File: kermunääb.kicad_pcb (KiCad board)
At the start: 2 copper layers, 140 parts, among them J1 Conn_01x05, SW1 RotaryEncoder_Switch, SW10 SW_SPST, SW11 SW_SPST, SW12 SW_SPST, SW13 SW_SPST, SW14 SW_SPST, SW15 SW_SPST, SW16 SW_SPST, SW17 SW_SPST, SW18 SW_SPST, SW19 SW_SPST, SW2 SW_SPST, SW20 SW_SPST, SW21 SW_SPST, SW22 SW_SPST, SW23 SW_SPST, SW24 SW_SPST, SW25 SW_SPST, SW26 SW_SPST, SW27 SW_SPST, SW28 SW_SPST, SW29 SW_SPST, SW3 SW_SPST, SW30 SW_SPST, SW31 SW_SPST, SW32 SW_SPST, SW33 SW_SPST, SW33A1 SW_SPST, SW34 SW_SPST, SW35 SW_SPST, SW36 SW_SPST, SW37 SW_SPST, SW38 SW_SPST, SW39 SW_SPST, SW4 SW_SPST, SW40 SW_SPST, SW41 SW_SPST, SW42 SW_SPST, SW43 SW_SPST, SW44 SW_SPST, SW45 SW_SPST, SW46 SW_SPST, SW47 SW_SPST, SW48 SW_SPST, SW49 SW_SPST, SW5 SW_SPST, SW50 SW_SPST, SW51 SW_SPST, SW52 SW_SPST, SW53 SW_SPST, SW54 SW_SPST, SW55 SW_SPST, SW56 SW_SPST, SW57 SW_SPST, SW58 SW_SPST, SW59 SW_SPST, SW6 SW_SPST, SW60 SW_SPST, SW61 SW_SPST, SW62 SW_SPST, SW63 SW_SPST, SW64 SW_SPST, SW65 SW_SPST, SW7 SW_SPST, SW8 SW_SPST, SW9 SW_SPST, U1 ProMicro

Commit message: change footprint for rotary header & add silk
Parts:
- J1: footprint Connector_PinSocket_2.54mm:PinSocket_1x05_P2.54mm_Horizontal -> Connector_PinSocket_2.54mm:PinSocket_1x05_P2.54mm_Vertical
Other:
- board text added: "A"
- board text added: "B"
- board text added: "GND"
- board text added: "SW1"
- board text added: "SW2"

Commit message: initial routing for right half and tweaks
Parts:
- added U2: ProMicro, promicro:ProMicro, B.Cu at (246.4, 69.8)
- J1: footprint Connector_PinSocket_2.54mm:PinSocket_1x05_P2.54mm_Vertical -> Connector_PinSocket_2.54mm:PinSocket_1x05_P2.54mm_Horizontal
- moved D7 7.00 mm to (153.4, 64.8), turned to 0 degrees
- moved D9 4.95 mm to (265.4, 64.8), turned to 180 degrees
- moved D8 4.95 mm to (246.4, 64.8), turned to 180 degrees
- moved D20 3.46 mm to (144.8, 82.8)
- moved D21 1.25 mm to (158.8, 82.5)
- moved U1 0.63 mm to (148.9, 69.8)
- moved D10 0.55 mm to (281.0, 61.8)
- moved D11 0.55 mm to (300.0, 61.8)
- moved D12 0.55 mm to (319.1, 61.8)
- moved D13 0.55 mm to (338.1, 61.8)
- moved D14 0.55 mm to (357.2, 61.8)
- renumbered SW33A1 to SW30A1
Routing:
- net /Col13: track 103.7 -> 202.7 mm
- net /Row5B: track 190.5 -> 279.3 mm
- net /Col12: track 149.3 -> 222.3 mm
- net /Row4B: track 121.4 -> 182.5 mm
- net /Col11: track 127.9 -> 182.4 mm
- net /Col10: track 123.9 -> 173.6 mm
- net /Row3B: track 114.3 -> 150.8 mm
- net /Col9: track 118.4 -> 145.3 mm
- net /Row1: track 109.4 -> 98.3 mm
- net Net-(D8-A): track 10.8 -> 2.70 mm
- net Net-(D9-A): track 10.8 -> 2.70 mm
- net Net-(D20-A): track 10.8 -> 2.96 mm
- net /Col5: track 105.3 -> 98.2 mm
- net /Col3: track 138.7 -> 143.9 mm
- net /Col4: track 141.2 -> 144.8 mm
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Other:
- board outline added: 148.2 x 105.2 mm

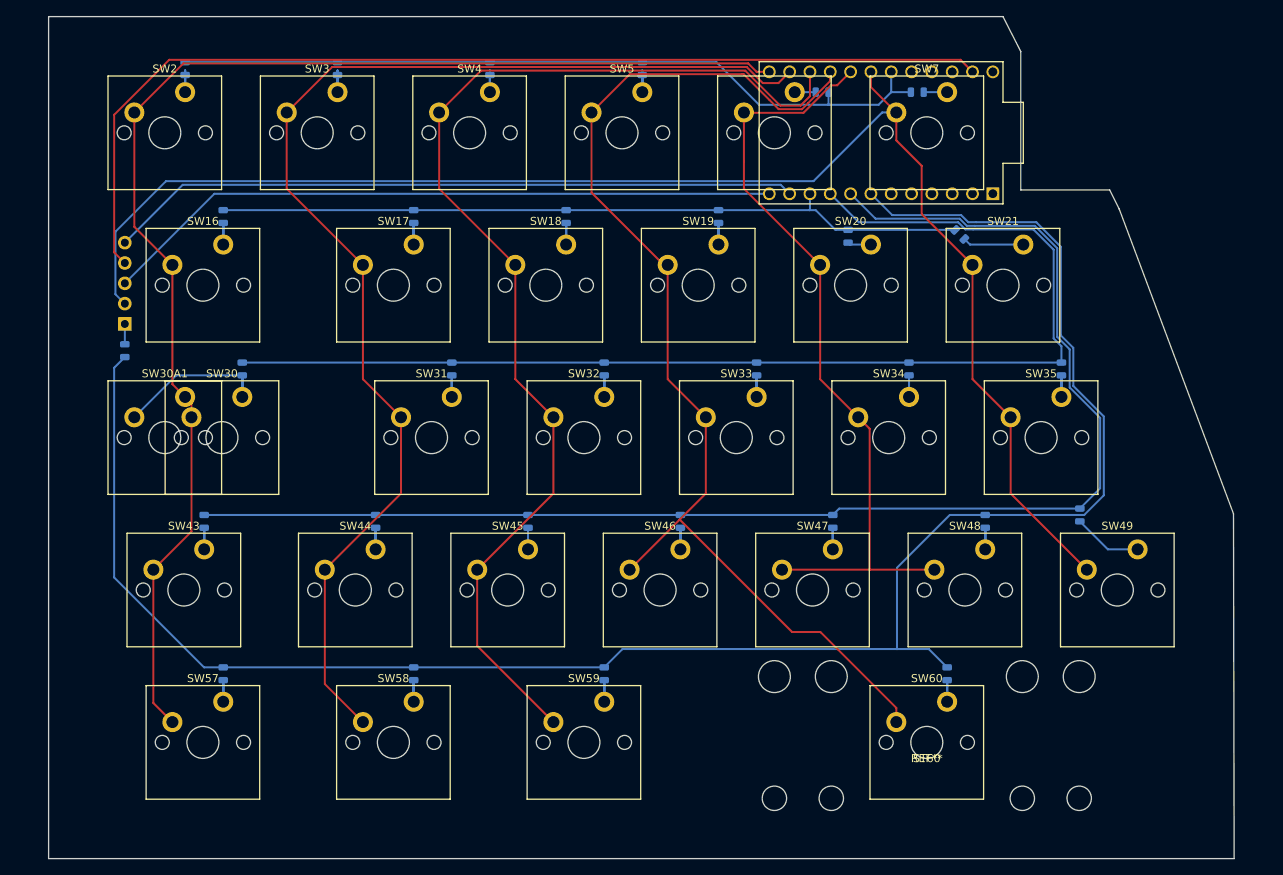
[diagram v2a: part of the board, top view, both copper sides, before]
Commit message: add initial edgecuts for left
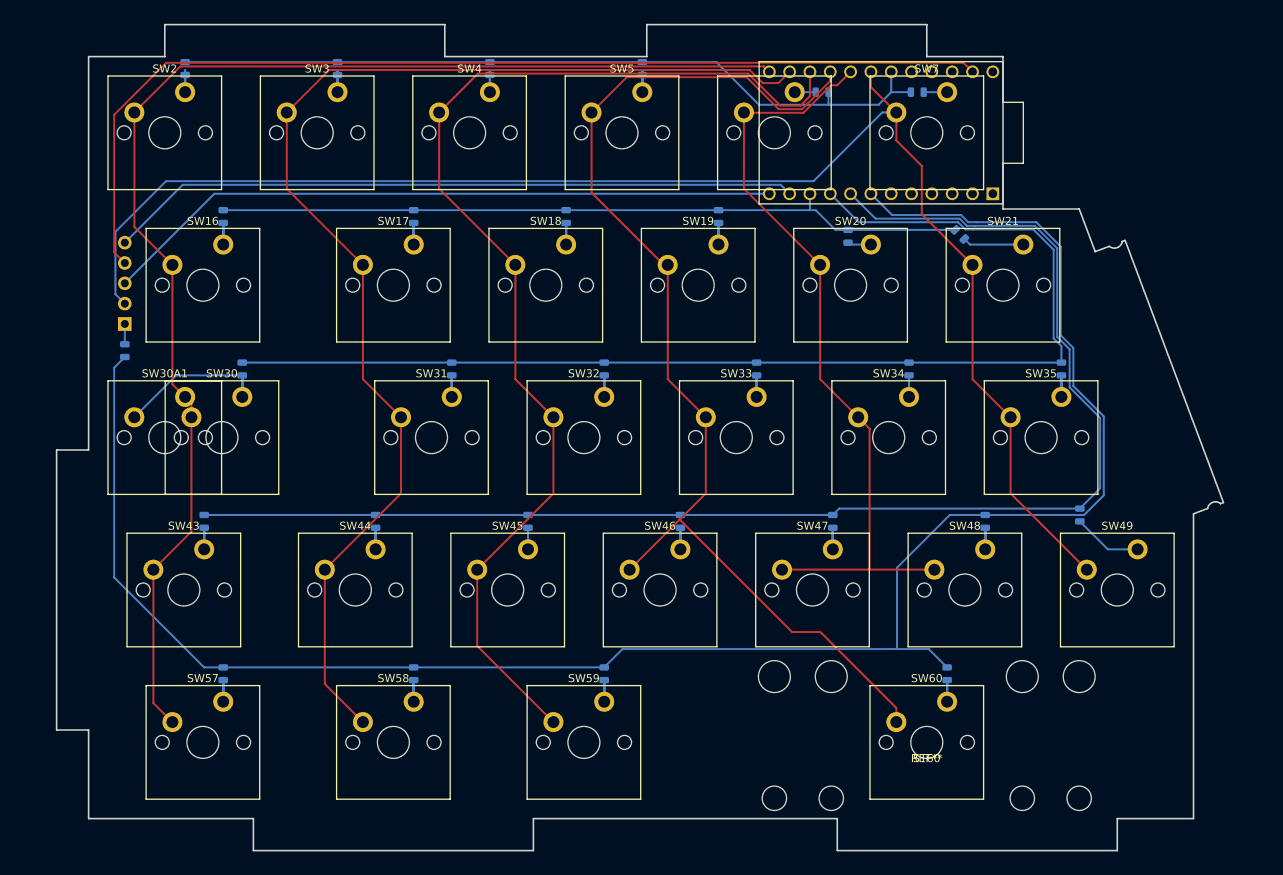
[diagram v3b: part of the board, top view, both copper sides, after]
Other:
- board size 148.2 x 105.2 mm -> 145.9 x 103.3 mm

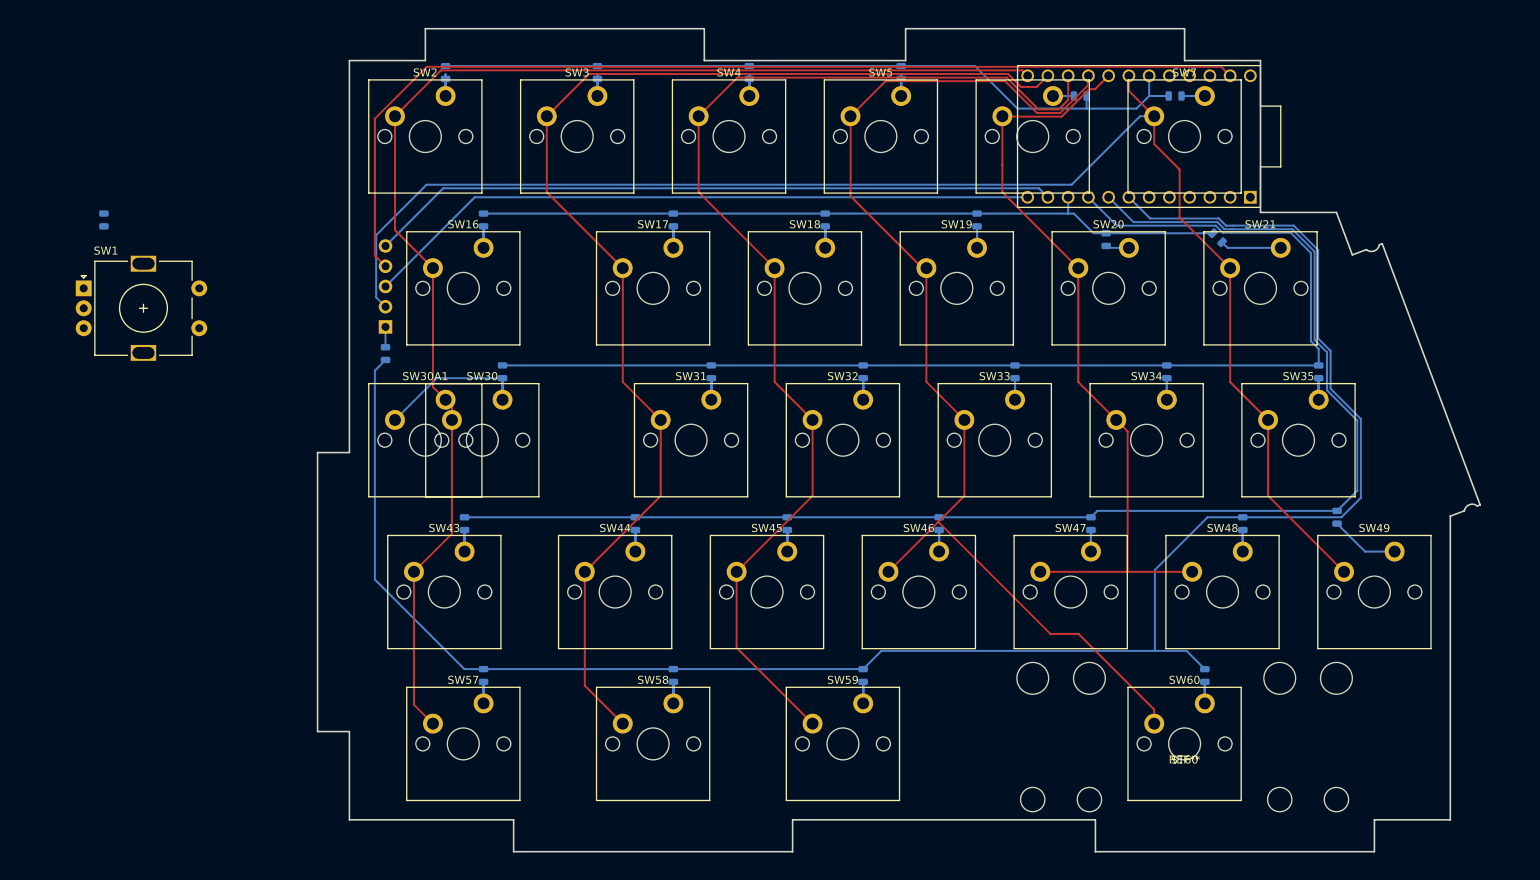
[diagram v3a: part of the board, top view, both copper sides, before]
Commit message: fix rotary encoder position & finetune left edgeCuts
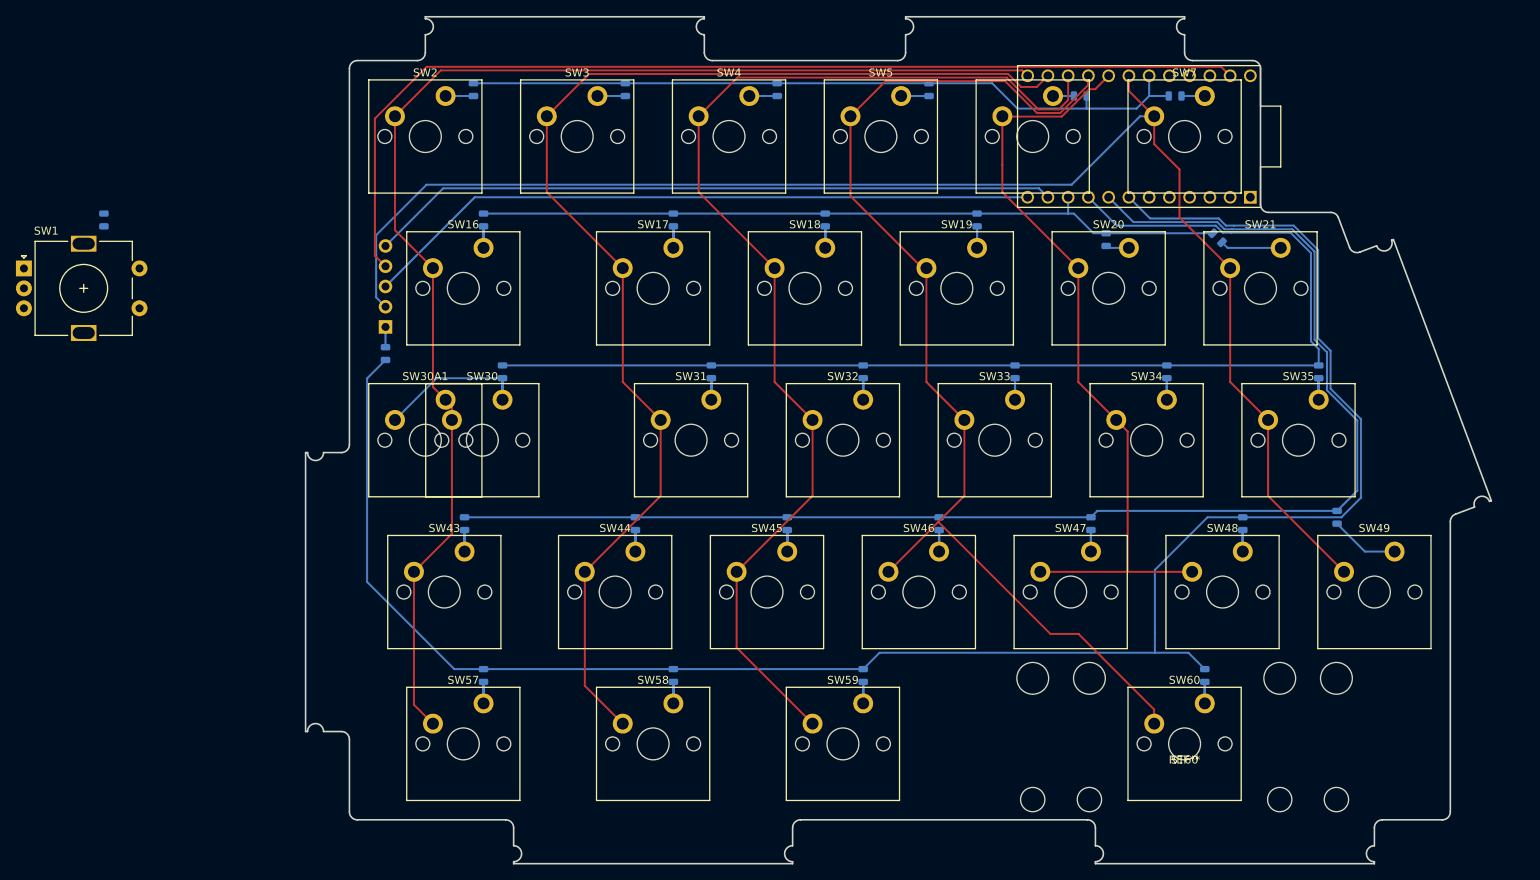
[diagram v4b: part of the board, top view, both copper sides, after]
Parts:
- moved SW1 7.91 mm to (9.01, 86.4)
- moved D4 4.11 mm to (103.5, 64.0)
- moved D3 4.10 mm to (84.5, 64.0)
- moved D2 4.10 mm to (65.4, 64.0)
- moved D5 4.10 mm to (122.6, 64.0)
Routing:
- net Net-(D5-A): track 10.8 -> 3.50 mm
- net Net-(D2-A): track 10.8 -> 3.50 mm
- net Net-(D3-A): track 10.8 -> 3.50 mm
- net Net-(D4-A): track 10.8 -> 3.50 mm
- net /Row1: track 98.3 -> 93.9 mm
- net /Row5: track 238.3 -> 239.9 mm
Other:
- board size 145.9 x 103.3 mm -> 148.8 x 106.3 mm

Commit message: small changes
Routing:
- net /Col6: track 186.7 -> 188.4 mm
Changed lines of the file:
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@@
   (segment (start 131.7625 67.31) (end 131.8025 67.35) (width 0.25) (layer "F.Cu") (net 77))
   (segment (start 147.637489 62.23) (end 147.637489 64.134989) (width 0.25) (layer "F.Cu") (net 78))
-  (segment (start 160.3375 86.36) (end 153.987 80.0095) (width 0.25) (layer "F.Cu") (net 78))
-  (segment (start 153.987 80.0095) (end 153.987 73.977) (width 0.25) (layer "F.Cu") (net 78))
+  (segment (start 155.995 72.995) (end 153.005 72.995) (width 0.25) (layer "F.Cu") (net 78))
+  (segment (start 159 76) (end 155.995 72.995) (width 0.25) (layer "F.Cu") (net 78))
+  (segment (start 160.3375 86.36) (end 159 85.0225) (width 0.25) (layer "F.Cu") (net 78))
+  (segment (start 159 85.0225) (end 159 76) (width 0.25) (layer "F.Cu") (net 78))
   (segment (start 150.8125 67.31) (end 147.637489 64.134989) (width 0.25) (layer "F.Cu") (net 78))
   (segment (start 165.1 105.41) (end 165.1 114.935) (width 0.25) (layer "F.Cu") (net 78))
@@
   (segment (start 165.1 114.935) (end 174.625 124.46) (width 0.25) (layer "F.Cu") (net 78))
   (segment (start 160.3375 100.6475) (end 165.1 105.41) (width 0.25) (layer "F.Cu") (net 78))
-  (segment (start 153.987 73.977) (end 150.8125 70.8025) (width 0.25) (layer "F.Cu") (net 78))
+  (segment (start 153.005 72.995) (end 150.8125 70.8025) (width 0.25) (layer "F.Cu") (net 78))
   (segment (start 150.8125 70.8025) (end 150.8125 67.31) (width 0.25) (layer "F.Cu") (net 78))
   (segment (start 54.375 91.205) (end 53.2 90.03) (width 0.25) (layer "B.Cu") (net 78))

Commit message: changed left side to nicenano .gitignore  and added battery wiring, still quite WIP
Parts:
- removed U1: ProMicro, promicro:ProMicro
- added J2: Conn_01x02_Pin, Connector_JST:JST_XH_S2B-XH-A-1_1x02_P2.50mm_Horizontal, B.Cu at (77.0, 79.0)
- added U3: ~, nice-nano-kicad:nice_nanov2_noextras, B.Cu at (146.4, 69.8)
- added U4: ~, nice-nano-kicad:nice_nanov2_noextras, F.Cu at (298.0, 211.0)
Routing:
- net /BAT+: track 0.00 -> 96.7 mm
- net /BAT-: track 0.00 -> 90.0 mm
- net /Col3: track 143.6 -> 137.1 mm
- net /Col6: track 188.4 -> 193.6 mm, vias 0 -> 1
- net /Col2: track 154.4 -> 151.6 mm
- net /Row5: track 239.9 -> 242.4 mm
- net /Row4: track 174.3 -> 176.8 mm
- net /Row3: track 147.7 -> 150.3 mm
- net /Col1: track 164.2 -> 161.6 mm
- net GND: track 129.5 -> 127.0 mm
- net /Col4: track 144.5 -> 146.2 mm
- net /Row1: track 93.9 -> 92.5 mm
- net /Row2: track 95.0 -> 96.2 mm
- net /RotB: track 86.6 -> 87.7 mm
- net /Col5: track 98.2 -> 97.6 mm
